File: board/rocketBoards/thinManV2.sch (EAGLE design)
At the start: 48 parts, among them J1 47346-0001

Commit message: thinManV2 changes
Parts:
- removed LED1: (no value), adafruit:LEDCHIPLED_0603
- removed R10, R7, R8: (no value), ELL-i-Passives:R0402
- removed S1: SWITCH-MOMENTARY-2-SMD-1101NE, SparkFun-Electromechanical:SWITCH-MOMENTARY-2-SMD-1101NE
- removed S4: DPDT, SparkFun-Electromechanical:SWITCH-DPDTAYZ0202
- removed U$3: MICROSD-CD, Sensors:MICROSD-CD
- added C2: 10uF, ELL-i-Passives:C0402
- added C4, C5: .1uF, ELL-i-Passives:C0402
- added D1, D2: (no value), SparkFun-LED:WS2812B
- added HIGHG: LPS331AP, Sensors:LPS331AP
- added R5: (no value), ELL-i-Passives:R0402
- added S2: (no value), SparkFun-Electromechanical:SWITCH-SPDT-SMD-A
- added U$1: RN4020, bluetooth:RN4020
- added U$7: S25FL127S, SparkFun-DigitalIC:S25FL127S
- JP2: value (none) -> M02JST-PTH-VERT; device SparkFun-Connectors:M04JST -> SparkFun-Connectors:M02JST-PTH-VERT
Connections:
- removed net BARO_INT2: U1.TRSTN/PIO0_14/ADC_6/CT32B1_MAT1/U1_TXD
- removed net HIGHG_INT2: U1.PIO1_13/U1_CTSN/SCT0_OUT3/R_22
- removed net INT2_A/G: U1.PIO0_17/U0_RTS/CT32B0_CAP0/U0_SCLK
- removed net N$16: R7.1, U$3.DAT2
- removed net N$19: S1.1, U1.PIO0_8/SSP0_MISO/CT16B0_MAT0/R_6
- removed net N$21: R10.2, U$3.DAT1
- new net N$6: D1.DOUT, D2.DIN
- new net PIXEL: D1.DIN, U1.TDI/PIO0_11/ADC_9/CT32B0_MAT3/U1_RTSN/U1_SCLK
- new net SSP1_RST: U$7.RST#
- net 3.3V: now also C2.1, C4.1, C5.1, D1.VDD, D2.VDD, HIGHG.CS, HIGHG.VCCA, HIGHG.VDD, HIGHG.VDD_IO, R5.2, U$7.VCC; no longer JP2.1, R10.1, R7.2, S4.6, U$3.VDD
- net GND: now also C2.2, C4.2, C5.2, D1.VSS, D2.VSS, HIGHG.GND, HIGHG.SDO/SA0, JP2.2; no longer JP2.3, R8.1, S1.2, S4.4, U$3.VSS
- net HIGHG_INT1: now also HIGHG.INT1; no longer U1.TDO/PIO0_13/ADC_7/CT32B1_MAT0/U1_RXD
- net I2C0_SCL: now also HIGHG.SCL/SPC
- net I2C0_SDA: now also HIGHG.SDA/SDI/SDO
- net LED_PIN2: no longer LED1.A
- net N$20: now also S2.O; no longer S4.1
- net N$4: now also R5.1, U$7.WP#; no longer LED1.C, R8.2
- net PIO0_1: now also JP2.1; no longer S4.5
- net SD_CD: no longer U$3.CD
- net SSP1_MISO: now also U$7.SO; no longer U$3.DAT0
- net SSP1_MOSI: now also U$7.SI; no longer U$3.CMD
- net SSP1_SCK: now also U$7.CLK; no longer U$3.CLK
- net SSP1_SSEL: now also U$7.CS#; no longer U$3.CD/DAT3
- net USB_VBUS: now also S2.S; no longer S4.3
- net VBUS: now also S2.P; no longer JP2.4, S4.2
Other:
- moved on the sheet: C19, C21

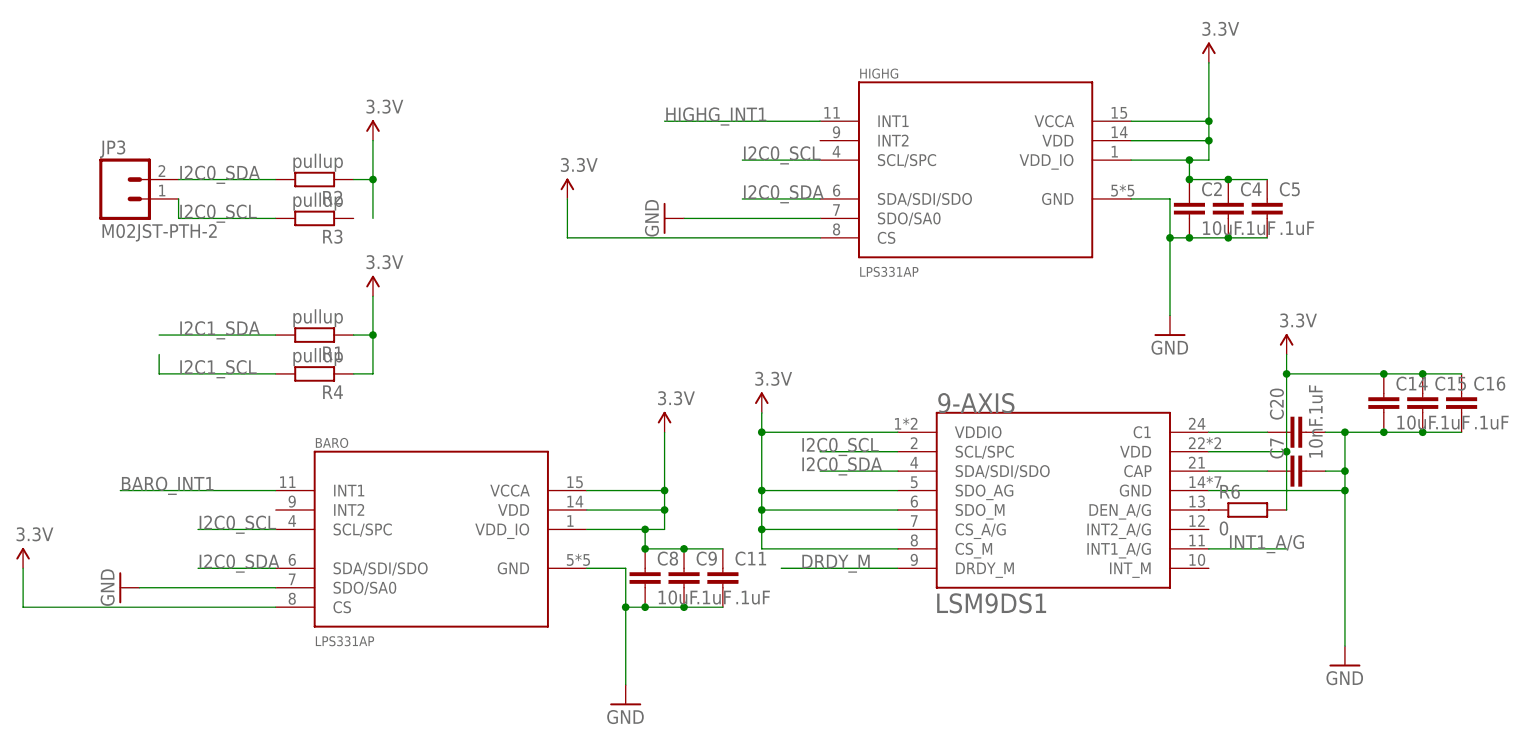
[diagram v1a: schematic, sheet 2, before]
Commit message: updated thinManV2 and lipoWing to use 0603 parts
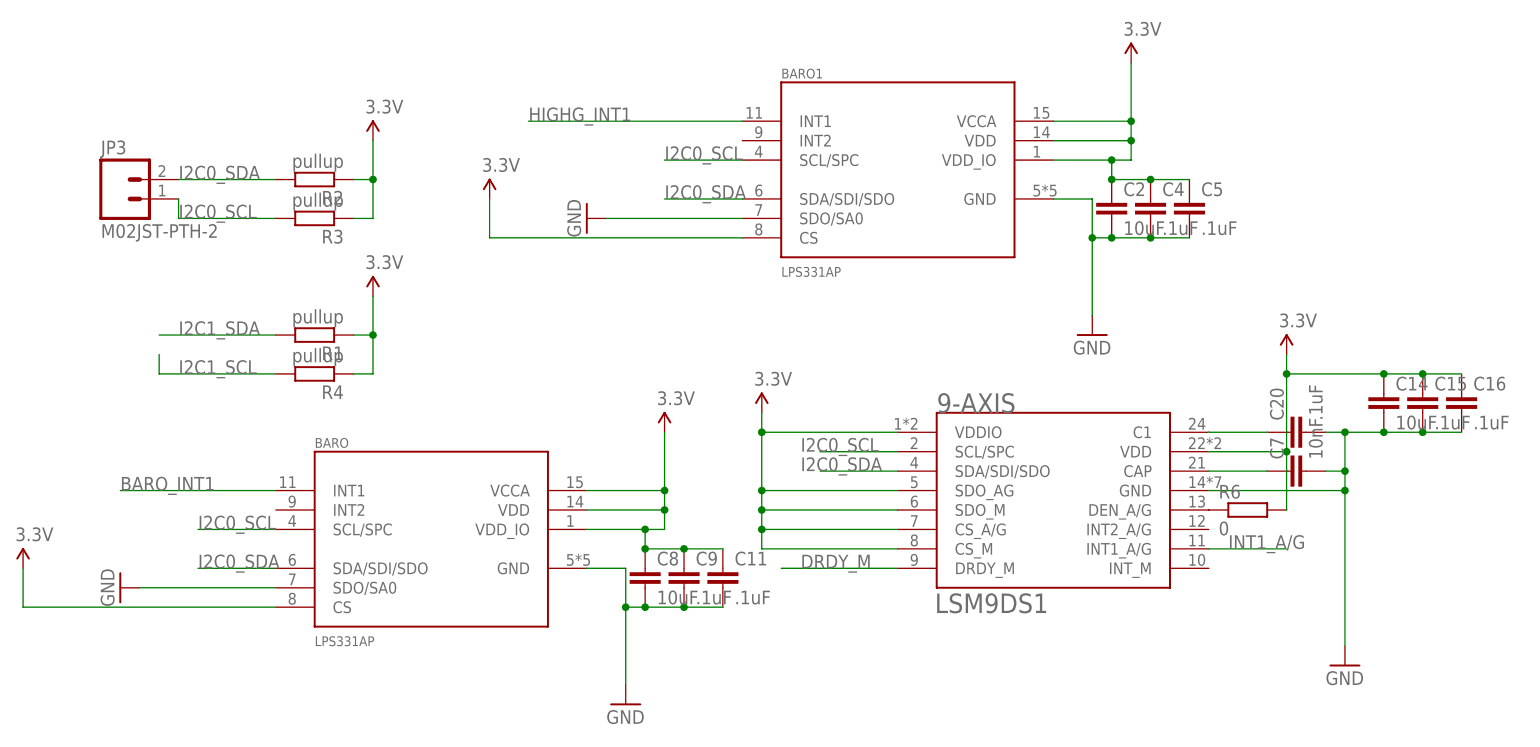
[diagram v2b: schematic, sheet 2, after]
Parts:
- removed C17: 1uF, ELL-i-Passives:C0402
- removed HIGHG: LPS331AP, Sensors:LPS331AP
- removed U$2: LDK220M33R, Sensors:LDK220M33R
- added BARO1: LPS331AP, Sensors:LPS331AP
- C1, C11, C14, C15, C16, C18, C19, C2, C20, C22, C24, C25, C26, C27, C28, C29, C3, C30, C4, C5, C7, C8, C9: device ELL-i-Passives:C0402 -> ELL-i-Passives:C0603
- C21: device ELL-i-Passives:CC1206 -> ELL-i-Passives:C0603
- R2, R3, R5, R6, R9: device ELL-i-Passives:R0402 -> ELL-i-Passives:R0603
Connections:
- removed net LED_PIN2: U1.PIO0_2/SSP0_SSEL/CT16B0_CAP0/R_0
- removed net N$18: U1.PIO1_21/U0_DCDN/SSP1_MISO/CT16B0_CAP1
- removed net N$22: U1.PIO2_2/U3_RTSN/U3_SCLK/SCT0_OUT1
- removed net SD_CD: U1.PIO2_5/U3_CTSN/SCT0_IN1
- new net BLE_RX: U$1.UART_TX, U1.PIO0_18/U0_RXD/CT32B0_MAT0
- new net BLE_TX: U$1.UART_RX, U1.PIO0_19/U0_TXD/CT32B0_MAT1
- new net BLE_WAKE: U$1.WAKE_HW, U1.PIO0_17/U0_RTS/CT32B0_CAP0/U0_SCLK
- net 3.3V: now also BARO1.CS, BARO1.VCCA, BARO1.VDD, BARO1.VDD_IO, R3.1, U$1.VDD; no longer HIGHG.CS, HIGHG.VCCA, HIGHG.VDD, HIGHG.VDD_IO, U$2.OUT
- net BARO_INT1: now also U1.PIO0_8/SSP0_MISO/CT16B0_MAT0/R_6; no longer U1.SWDIO/PIO0_15/ADC_3/CT32B1_MAT2
- net DRDY_M: now also U1.PIO2_7/SSP0_SCK/SCT0_OUT2; no longer U1.PIO0_19/U0_TXD/CT32B0_MAT1
- net GND: now also BARO1.GND, BARO1.SDO/SA0, U$1.GND; no longer C17.2, HIGHG.GND, HIGHG.SDO/SA0, U$2.GND
- net HIGHG_INT1: now also BARO1.INT1, U1.PIO0_9/SSP0_MOSI/CT16B0_MAT1/R_7; no longer HIGHG.INT1
- net I2C0_SCL: now also BARO1.SCL/SPC; no longer HIGHG.SCL/SPC
- net I2C0_SDA: now also BARO1.SDA/SDI/SDO; no longer HIGHG.SDA/SDI/SDO
- net INT1_A/G: now also U1.PIO0_6/USB_CONNECTN/SSP0_SCK/R_4; no longer U1.PIO0_18/U0_RXD/CT32B0_MAT0
- net PIXEL: now also U1.SWCLK/PIO0_10/SSP0_SCK/CT16B0_MAT2; no longer U1.TDI/PIO0_11/ADC_9/CT32B0_MAT3/U1_RTSN/U1_SCLK
- net SSP1_MISO: now also U1.PIO1_21/U0_DCDN/SSP1_MISO/CT16B0_CAP1; no longer U1.PIO0_22/ADC_11/CT16B1_CAP1/SSP1_MISO
- net SSP1_RST: now also U1.PIO2_2/U3_RTSN/U3_SCLK/SCT0_OUT1
- net SSP1_SSEL: now also U1.PIO1_23/CT16B1_MAT1/SSP1_SSEL/U2_TXD; no longer U1.PIO0_16/ADC_2/CT32B1_MAT3/R_8/WAKEUP
- net VBUS: no longer C17.1, U$2.EN, U$2.IN
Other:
- moved on the sheet: C2, C4, C5
